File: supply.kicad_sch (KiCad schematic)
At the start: 10 parts, among them U2 AP62301WU-7

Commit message: Update L1 symbol
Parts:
- L1: symbol antmicroFixedInductors:SRP3212A-1R0M -> antmicroFixedInductors:L_1u_5.5A_SRP3212
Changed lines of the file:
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@@
     (pin "1")
   )
-  (symbol (lib_id "antmicroFixedInductors:SRP3212A-1R0M") (at 218.44 142.24 0) (unit 1)
+  (symbol (lib_id "antmicroFixedInductors:L_1u_5.5A_SRP3212") (at 218.44 142.24 0) (unit 1)
     (in_bom yes) (on_board yes)
     (property "Reference" "L1" (id 0) (at 223.012 134.62 0)
@@
       (effects (font (size 1.27 1.27) (thickness 0.15)) (justify left bottom) hide)
     )
-    (property "Datasheet" "https://www.mouser.pl/datasheet/2/54/srp3212-2948733.pdf" (id 3) (at 229.87 157.48 0)
+    (property "Datasheet" "https://www.mouser.pl/datasheet/2/54/SRP3212A-3011944.pdf" (id 3) (at 229.87 157.48 0)
       (effects (font (size 1.27 1.27) (thickness 0.15)) (justify left bottom) hide)
     )

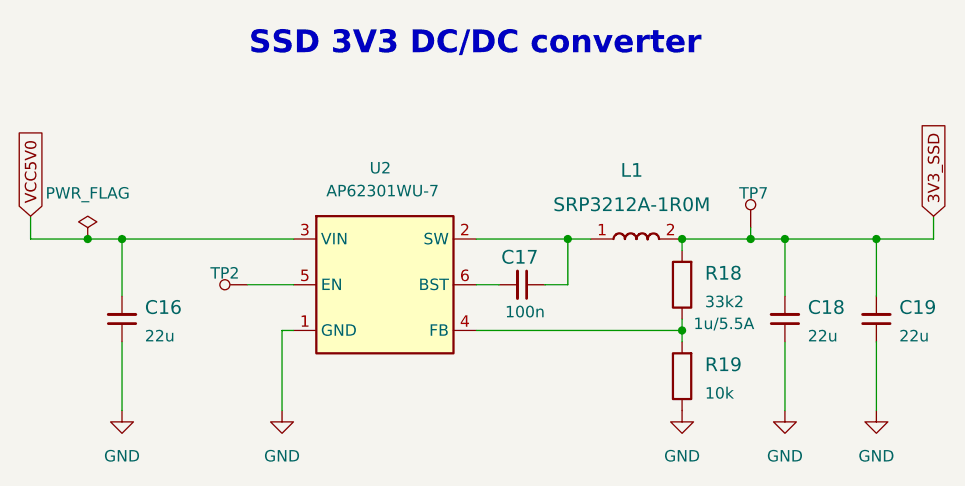
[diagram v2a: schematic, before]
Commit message: Update R5, R9, R10, R11, R12, R13, R14, R19, R55, R65 symbol and footprint
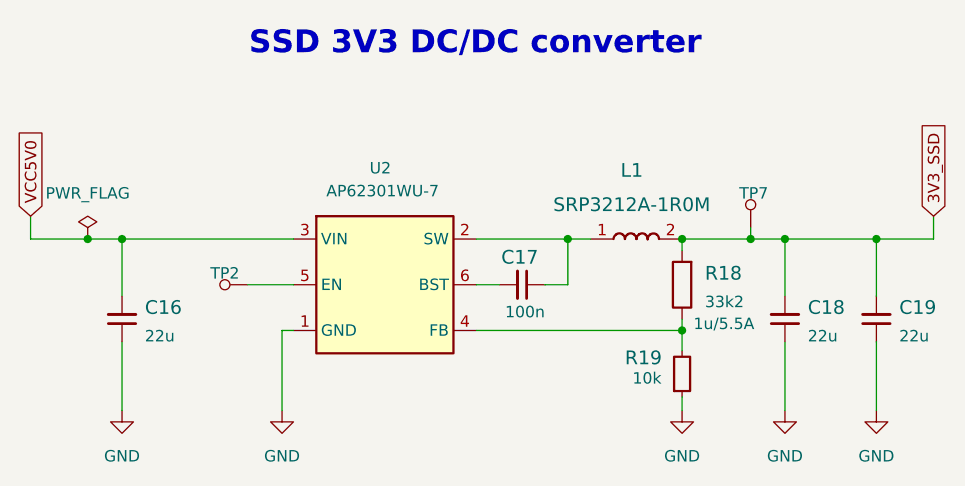
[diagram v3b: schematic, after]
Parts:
- R19: footprint scalenode-cm4-baseboard-footprints:0402-res -> antmicro-footprints:R_0402_1005Metric; symbol scalenode-cm4-baseboard:R_10k_0402 -> antmicroResistors0402:R_10k_0402; Author (none) -> Antmicro; License (none) -> Apache-2.0; MPN CRCW040210K0FKEDHP -> CR0402-FX-1002GLF; Manufacturer VISHAY -> Bourns; Tolerance (none) -> 1%
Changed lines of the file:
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@@
     (stroke (width 0) (type default) (color 0 0 0 0))
   )
-  (wire (pts (xy 228.6 152.4) (xy 228.6 153.67))
+  (wire (pts (xy 228.6 152.4) (xy 228.6 154.686))
     (stroke (width 0) (type default) (color 0 0 0 0))
   )
@@
   )
   (wire (pts (xy 250.19 142.24) (xy 250.19 148.59))
+    (stroke (width 0) (type default) (color 0 0 0 0))
+  )
+  (wire (pts (xy 228.6 159.766) (xy 228.6 161.29))
     (stroke (width 0) (type default) (color 0 0 0 0))
   )
@@
     (pin "2")
   )
-  (symbol (lib_id "scalenode-cm4-baseboard:R_10k_0402") (at 228.6 157.48 90) (unit 1)
-    (in_bom yes) (on_board yes) (fields_autoplaced)
-    (property "Reference" "R19" (id 0) (at 231.14 156.21 90)
+  (symbol (lib_id "antmicroResistors0402:R_10k_0402") (at 228.6 159.766 90) (unit 1)
+    (in_bom yes) (on_board yes)
+    (property "Reference" "R19" (id 0) (at 222.25 155.448 90)
       (effects (font (size 1.524 1.524)) (justify right))
     )
-    (property "Value" "R_10k_0402" (id 1) (at 232.41 157.48 0)
+    (property "Value" "R_10k_0402" (id 1) (at 232.41 159.766 0)
       (effects (font (size 1.524 1.524)) hide)
     )
-    (property "Footprint" "scalenode-cm4-baseboard-footprints:0402-res" (id 2) (at 223.52 152.4 0)
-      (effects (font (size 1.524 1.524)) (justify left) hide)
-    )
-    (property "Datasheet" "" (id 3) (at 228.6 157.48 0)
-      (effects (font (size 1.27 1.27)) hide)
-    )
-    (property "Manufacturer" "VISHAY" (id 4) (at 218.44 152.4 0)
-      (effects (font (size 1.524 1.524)) (justify left) hide)
-    )
-    (property "MPN" "CRCW040210K0FKEDHP" (id 5) (at 220.98 152.4 0)
-      (effects (font (size 1.524 1.524)) (justify left) hide)
-    )
-    (property "Val" "10k" (id 6) (at 231.14 159.3849 90)
-      (effects (font (size 1.27 1.27)) (justify right))
+    (property "Footprint" "antmicro-footprints:R_0402_1005Metric" (id 2) (at 243.84 139.446 0)
+      (effects (font (size 1.27 1.27) (thickness 0.15)) (justify left bottom) hide)
+    )
+    (property "Datasheet" "https://www.bourns.com/docs/product-datasheets/cr.pdf" (id 3) (at 246.38 139.446 0)
+      (effects (font (size 1.27 1.27) (thickness 0.15)) (justify left bottom) hide)
+    )
+    (property "Manufacturer" "Bourns" (id 4) (at 251.46 139.446 0)
+      (effects (font (size 1.27 1.27) (thickness 0.15)) (justify left bottom) hide)
+    )
+    (property "MPN" "CR0402-FX-1002GLF" (id 5) (at 248.92 139.446 0)
+      (effects (font (size 1.27 1.27) (thickness 0.15)) (justify left bottom) hide)
+    )
+    (property "Val" "10k" (id 6) (at 226.314 156.972 90)
+      (effects (font (size 1.27 1.27) (thickness 0.15)) (justify left bottom))
+    )
+    (property "License" "Apache-2.0" (id 7) (at 254 139.446 0)
+      (effects (font (size 1.27 1.27) (thickness 0.15)) (justify left bottom) hide)
+    )
+    (property "Author" "Antmicro" (id 8) (at 256.54 139.446 0)
+      (effects (font (size 1.27 1.27) (thickness 0.15)) (justify left bottom) hide)
+    )
+    (property "Tolerance" "1%" (id 9) (at 238.76 139.446 0)
+      (effects (font (size 1.27 1.27)) (justify left bottom) hide)
     )
     (pin "1")

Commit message: Update R18 symbol and footprint
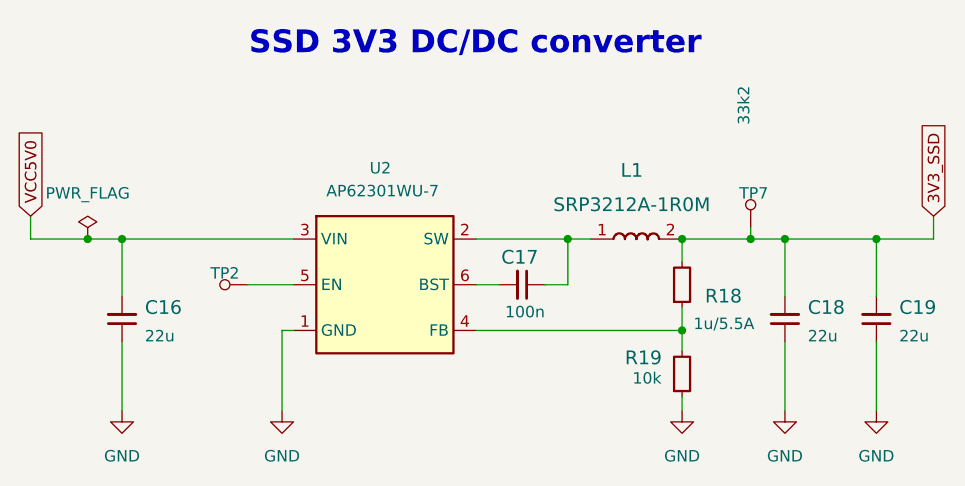
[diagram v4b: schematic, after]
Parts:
- R18: footprint scalenode-cm4-baseboard-footprints:0402-res -> antmicro-footprints:R_0402_1005Metric; symbol scalenode-cm4-baseboard:R_33k2_0402 -> antmicroResistors0402:R_33k2_0402; Author (none) -> Antmicro; License (none) -> Apache-2.0; MPN ERJ2RKF3322X -> CR0402-FX-3322GLF; Manufacturer PANASONIC -> Bourns; Tolerance (none) -> 1%
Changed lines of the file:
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@@
     (stroke (width 0) (type default) (color 0 0 0 0))
   )
-  (wire (pts (xy 228.6 151.13) (xy 228.6 152.4))
+  (wire (pts (xy 228.6 149.86) (xy 228.6 152.4))
     (stroke (width 0) (type default) (color 0 0 0 0))
   )
@@
     (stroke (width 0) (type default) (color 0 0 0 0))
   )
-  (wire (pts (xy 228.6 143.51) (xy 228.6 142.24))
+  (wire (pts (xy 228.6 142.24) (xy 228.6 144.78))
     (stroke (width 0) (type default) (color 0 0 0 0))
   )
@@
     (pin "1")
   )
-  (symbol (lib_id "scalenode-cm4-baseboard:R_33k2_0402") (at 228.6 147.32 90) (unit 1)
+  (symbol (lib_id "antmicroResistors0402:R_33k2_0402") (at 228.6 149.86 90) (unit 1)
     (in_bom yes) (on_board yes) (fields_autoplaced)
-    (property "Reference" "R18" (id 0) (at 231.14 146.05 90)
+    (property "Reference" "R18" (id 0) (at 231.14 148.59 90)
       (effects (font (size 1.524 1.524)) (justify right))
     )
-    (property "Value" "R_33k2_0402" (id 1) (at 232.41 147.32 0)
+    (property "Value" "R_33k2_0402" (id 1) (at 232.41 149.86 0)
       (effects (font (size 1.524 1.524)) hide)
     )
-    (property "Footprint" "scalenode-cm4-baseboard-footprints:0402-res" (id 2) (at 223.52 142.24 0)
-      (effects (font (size 1.524 1.524)) (justify left) hide)
-    )
-    (property "Datasheet" "" (id 3) (at 228.6 147.32 0)
-      (effects (font (size 1.27 1.27)) hide)
-    )
-    (property "Manufacturer" "PANASONIC" (id 4) (at 218.44 142.24 0)
-      (effects (font (size 1.524 1.524)) (justify left) hide)
-    )
-    (property "MPN" "ERJ2RKF3322X" (id 5) (at 220.98 142.24 0)
-      (effects (font (size 1.524 1.524)) (justify left) hide)
-    )
-    (property "Val" "33k2" (id 6) (at 231.14 149.2249 90)
-      (effects (font (size 1.27 1.27)) (justify right))
+    (property "Footprint" "antmicro-footprints:R_0402_1005Metric" (id 2) (at 243.84 129.54 0)
+      (effects (font (size 1.27 1.27) (thickness 0.15)) (justify left bottom) hide)
+    )
+    (property "Datasheet" "https://www.bourns.com/docs/product-datasheets/cr.pdf" (id 3) (at 246.38 129.54 0)
+      (effects (font (size 1.27 1.27) (thickness 0.15)) (justify left bottom) hide)
+    )
+    (property "Manufacturer" "Bourns" (id 4) (at 251.46 129.54 0)
+      (effects (font (size 1.27 1.27) (thickness 0.15)) (justify left bottom) hide)
+    )
+    (property "MPN" "CR0402-FX-3322GLF" (id 5) (at 248.92 129.54 0)
+      (effects (font (size 1.27 1.27) (thickness 0.15)) (justify left bottom) hide)
+    )
+    (property "Val" "33k2" (id 6) (at 236.22 129.54 0)
+      (effects (font (size 1.27 1.27) (thickness 0.15)) (justify left bottom))
+    )
+    (property "License" "Apache-2.0" (id 7) (at 254 129.54 0)
+      (effects (font (size 1.27 1.27) (thickness 0.15)) (justify left bottom) hide)
+    )
+    (property "Author" "Antmicro" (id 8) (at 256.54 129.54 0)
+      (effects (font (size 1.27 1.27) (thickness 0.15)) (justify left bottom) hide)
+    )
+    (property "Tolerance" "1%" (id 9) (at 238.76 129.54 0)
+      (effects (font (size 1.27 1.27)) (justify left bottom) hide)
     )
     (pin "1")

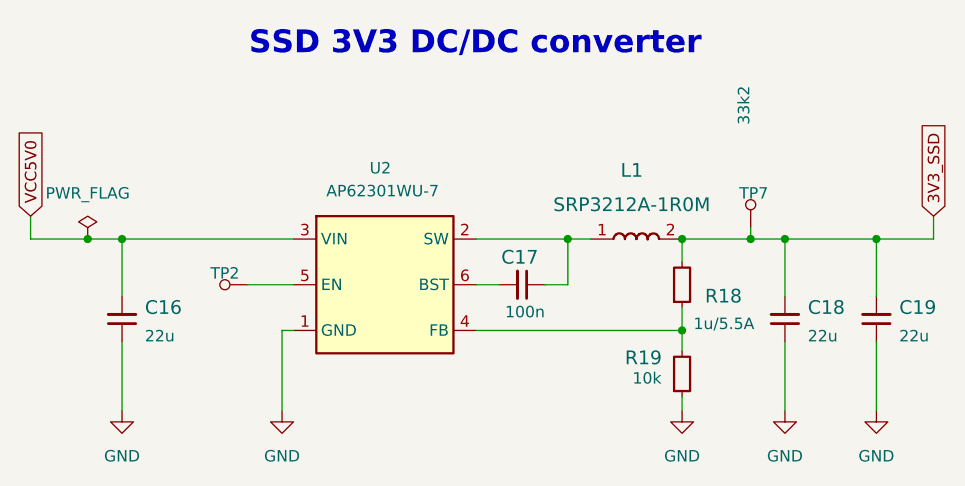
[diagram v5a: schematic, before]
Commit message: Update TP2, TP3, TP4, TP5, TP6, TP7 symbol and footprint
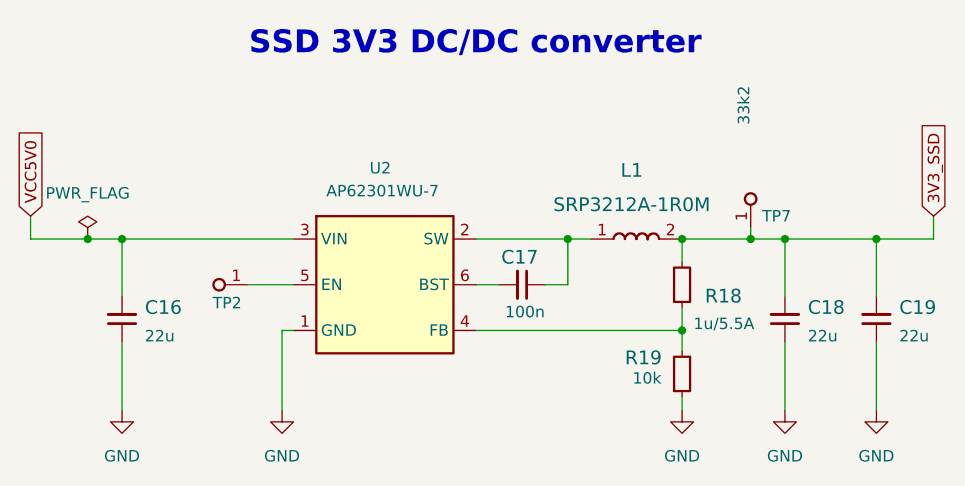
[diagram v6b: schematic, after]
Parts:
- TP2, TP7: footprint scalenode-cm4-baseboard-footprints:Testpoint_smd_1mm -> antmicro-footprints:Testpoint_smd_1mm; symbol scalenode-cm4-baseboard:TP_SMD1MM -> antmicroTestPoints:TP_1mm_SMD; Author (none) -> Antmicro; License (none) -> Apache-2.0
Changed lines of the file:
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@@
     (pin "2")
   )
-  (symbol (lib_id "scalenode-cm4-baseboard:TP_SMD1MM") (at 236.22 138.43 180) (unit 1)
+  (symbol (lib_id "antmicroTestPoints:TP_1mm_SMD") (at 236.22 140.97 90) (unit 1)
     (in_bom yes) (on_board yes)
-    (property "Reference" "TP7" (id 0) (at 234.95 137.16 0)
+    (property "Reference" "TP7" (id 0) (at 237.49 139.7 90)
       (effects (font (size 1.27 1.27)) (justify right))
     )
-    (property "Value" "TP_SMD1MM" (id 1) (at 236.22 135.89 0)
+    (property "Value" "TP_SMD1MM" (id 1) (at 238.76 140.97 0)
       (effects (font (size 1.27 1.27)) hide)
     )
-    (property "Footprint" "scalenode-cm4-baseboard-footprints:Testpoint_smd_1mm" (id 2) (at 231.14 143.51 0)
-      (effects (font (size 1.524 1.524)) (justify left) hide)
+    (property "Footprint" "antmicro-footprints:Testpoint_smd_1mm" (id 2) (at 246.38 125.73 0)
+      (effects (font (size 1.27 1.27) (thickness 0.15)) (justify left bottom) hide)
     )
-    (property "Datasheet" "" (id 3) (at 231.14 146.05 0)
-      (effects (font (size 1.524 1.524)) (justify left) hide)
+    (property "Datasheet" "" (id 3) (at 248.92 125.73 0)
+      (effects (font (size 1.27 1.27) (thickness 0.15)) (justify left bottom) hide)
+    )
+    (property "Author" "Antmicro" (id 4) (at 251.46 125.73 0)
+      (effects (font (size 1.27 1.27) (thickness 0.15)) (justify left bottom) hide)
+    )
+    (property "License" "Apache-2.0" (id 5) (at 254 125.73 0)
+      (effects (font (size 1.27 1.27) (thickness 0.15)) (justify left bottom) hide)
     )
     (pin "1")
@@
     (pin "2")
   )
-  (symbol (lib_id "scalenode-cm4-baseboard:TP_SMD1MM") (at 177.8 147.32 270) (unit 1)
+  (symbol (lib_id "antmicroTestPoints:TP_1mm_SMD") (at 180.34 147.32 180) (unit 1)
     (in_bom yes) (on_board yes)
-    (property "Reference" "TP2" (id 0) (at 177.8 146.05 90))
-    (property "Value" "TP_SMD1MM" (id 1) (at 175.26 147.32 0)
+    (property "Reference" "TP2" (id 0) (at 178.054 149.352 0))
+    (property "Value" "TP_SMD1MM" (id 1) (at 180.34 144.78 0)
       (effects (font (size 1.27 1.27)) hide)
     )
-    (property "Footprint" "scalenode-cm4-baseboard-footprints:Testpoint_smd_1mm" (id 2) (at 182.88 152.4 0)
-      (effects (font (size 1.524 1.524)) (justify left) hide)
+    (property "Footprint" "antmicro-footprints:Testpoint_smd_1mm" (id 2) (at 165.1 137.16 0)
+      (effects (font (size 1.27 1.27) (thickness 0.15)) (justify left bottom) hide)
     )
-    (property "Datasheet" "" (id 3) (at 185.42 152.4 0)
-      (effects (font (size 1.524 1.524)) (justify left) hide)
+    (property "Datasheet" "" (id 3) (at 165.1 134.62 0)
+      (effects (font (size 1.27 1.27) (thickness 0.15)) (justify left bottom) hide)
+    )
+    (property "Author" "Antmicro" (id 4) (at 165.1 132.08 0)
+      (effects (font (size 1.27 1.27) (thickness 0.15)) (justify left bottom) hide)
+    )
+    (property "License" "Apache-2.0" (id 5) (at 165.1 129.54 0)
+      (effects (font (size 1.27 1.27) (thickness 0.15)) (justify left bottom) hide)
     )
     (pin "1")
